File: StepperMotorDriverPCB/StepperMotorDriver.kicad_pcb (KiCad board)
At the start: 4 copper layers, 44.8 x 38.3 mm, 57 parts, among them IC2 TMC2209-LA, J1 Conn_01x02_Pin, J2 Conn_01x01_Pin, J3 Conn_01x01_Pin, J4 Conn_01x04_Socket, J5 USB_C_Receptacle_USB2.0_14P, J6 Conn_01x04_Pin, J7 Conn_01x02_Pin, J8 Conn_01x01_Pin, J9 Conn_01x01_Pin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

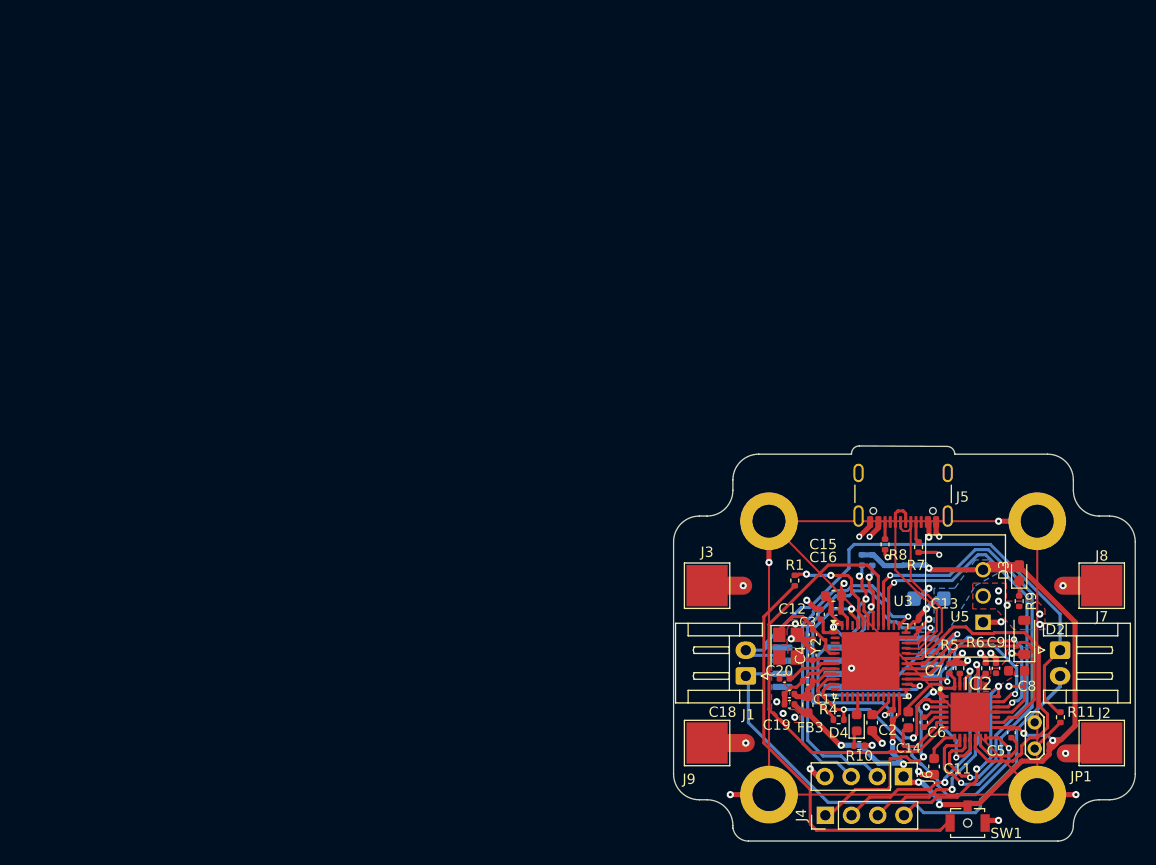
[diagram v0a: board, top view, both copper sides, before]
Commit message: Replaced Microcontrollers and Power Distribution System
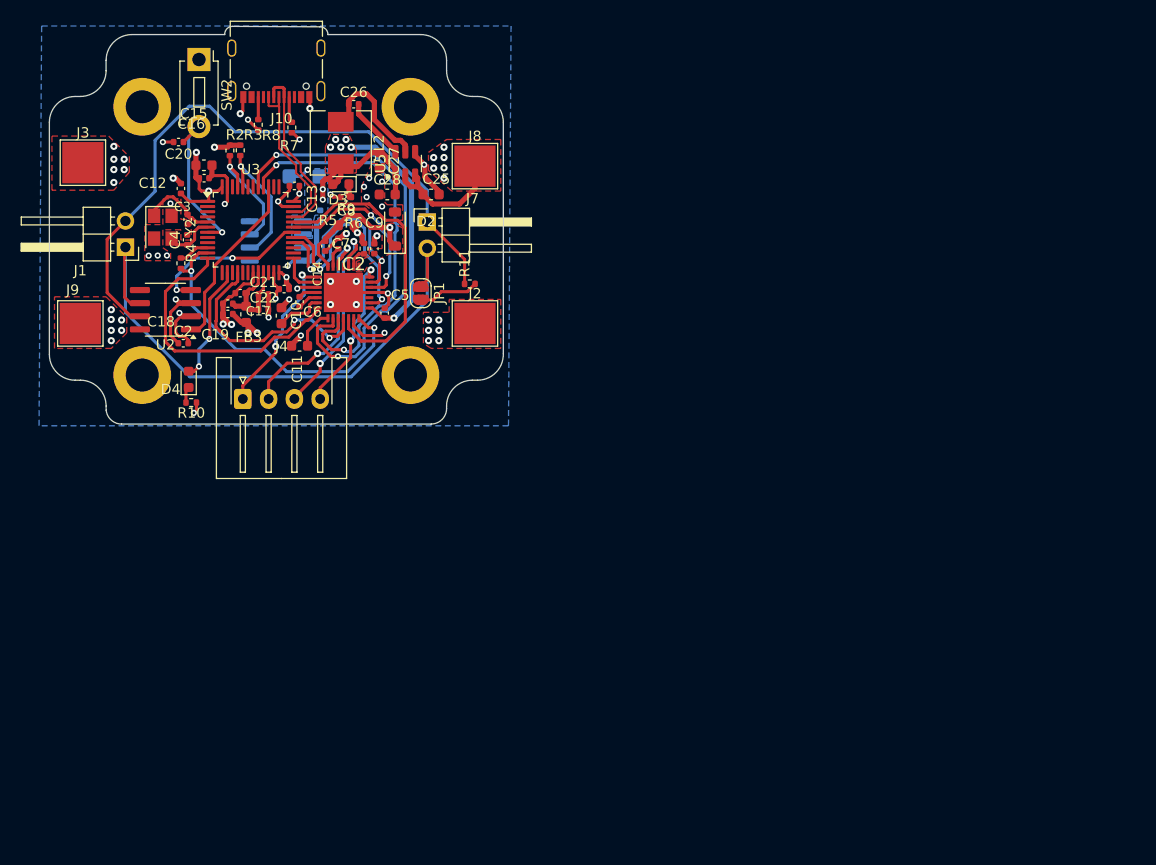
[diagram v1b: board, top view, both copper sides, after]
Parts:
- removed J5: USB_C_Receptacle_USB2.0_14P, Connector_USB:USB_C_Receptacle_GCT_USB4105-xx-A_16P_TopMnt_Horizontal
- removed J6: Conn_01x04_Pin, Connector_PinHeader_2.54mm:PinHeader_1x04_P2.54mm_Vertical
- removed R1: 10K, Resistor_SMD:R_0402_1005Metric
- removed SW1: SW_SPDT, Button_Switch_SMD:SW_SPST_B3U-1100P-B
- added C21: 100n, Capacitor_SMD:C_0402_1005Metric, F.Cu at (72.0, 68.5)
- added C22: 1u, Capacitor_SMD:C_0402_1005Metric, F.Cu at (72.0, 70.0)
- added C25: 10uF, Capacitor_SMD:C_0603_1608Metric, F.Cu at (88.2, 58.8)
- added C26: 100nF, Capacitor_SMD:C_0402_1005Metric, F.Cu at (80.8, 50.1)
- added C27: 22uF, Capacitor_SMD:C_0603_1608Metric, F.Cu at (83.2, 55.6)
- added C28: 22uF, Capacitor_SMD:C_0603_1608Metric, F.Cu at (84.0, 58.8)
- added J10: USB_C_Receptacle_USB2.0_16P, Connector_USB:USB_C_Receptacle_Palconn_UTC16-G, F.Cu at (73.2, 46.9)
- added L2: 4.7uF, Inductor_SMD:L_Chilisin_BMRA00050530, F.Cu at (79.5, 53.8)
- added SW2: SW_SPST, Button_Switch_THT:SW_PUSH_1P1T_6x3.5mm_H5.0_APEM_MJTP1250, F.Cu at (65.8, 45.8)
- C2: value 2.2uF -> 100nF; footprint Capacitor_SMD:C_0603_1608Metric -> Capacitor_SMD:C_0402_1005Metric
- C20: value 100n -> 0.1u
- J1, J7: footprint Connector_JST:JST_EH_S2B-EH_1x02_P2.50mm_Horizontal -> Connector_PinHeader_2.54mm:PinHeader_1x02_P2.54mm_Horizontal
- J4: footprint Connector_PinHeader_2.54mm:PinHeader_1x04_P2.54mm_Vertical -> Connector_JST:JST_XH_S4B-XH-A-1_1x04_P2.50mm_Horizontal
- JP1: footprint TestPoint:TestPoint_2Pads_Pitch2.54mm_Drill0.8mm -> Jumper:SolderJumper-2_P1.3mm_Open_RoundedPad1.0x1.5mm
- R2, R3: value 5K -> 5.1k; moved to F.Cu
- R9: value 1k5 -> 1.5k
- U2: moved to F.Cu
- U3: value STM32F423CHU6 -> STM32G473CBTx; footprint Package_DFN_QFN:QFN-48-1EP_7x7mm_P0.5mm_EP5.6x5.6mm -> Package_QFP:LQFP-48_7x7mm_P0.5mm
- U5: value TSR1-2433E -> AP63203WU; footprint Converter_DCDC:Converter_DCDC_TRACO_TSR1-xxxxE_THT -> Package_TO_SOT_SMD:TSOT-23-6
- moved C20 78.4 mm to (63.8, 53.8), turned to 180 degrees
- moved C8 78.0 mm to (80.0, 61.8)
- moved R4 77.6 mm to (64.0, 65.5), turned to 90 degrees
- moved C2 76.2 mm to (64.2, 73.2), turned to 0 degrees
- moved R9 76.1 mm to (80.0, 59.1), turned to 180 degrees
- moved D3 75.8 mm to (79.5, 57.8), turned to 180 degrees
- moved C12 74.5 mm to (64.0, 58.2)
- moved C16 74.3 mm to (66.2, 57.2)
- moved J7 74.1 mm to (87.9, 61.5), turned to 0 degrees
- moved C15 73.9 mm to (66.2, 56.0)
- moved C13 73.9 mm to (75.0, 58.0), turned to 180 degrees
- moved R2 73.8 mm to (68.8, 54.6)
- moved C11 73.8 mm to (75.5, 73.5), turned to 0 degrees
- moved C1 73.5 mm to (77.5, 60.9)
- moved U3 73.2 mm to (70.8, 62.2)
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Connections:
- C2 pad 1: Net-(U3-VCAP_1) -> +3V3
- C20 pad 1: GND -> Net-(SW2-B)
- C20 pad 2: /RST -> GND
- U3 pad 12: unconnected-(U3-PA2-Pad12) -> /MOT_SPREAD
- U3 pad 14: unconnected-(U3-PA4-Pad14) -> Net-(D4-A)
- U3 pad 16: Net-(D4-A) -> /MOT_DIAG
- U3 pad 19: unconnected-(U3-PB1-Pad19) -> GND
- U3 pad 20: unconnected-(U3-PB2-Pad20) -> +3.3VA
- U3 pad 21: unconnected-(U3-PB10-Pad21) -> +3.3VA
- U3 pad 22: Net-(U3-VCAP_1) -> unconnected-(U3-PB10-Pad22)
- U3 pad 25: /CAN_TX -> /MOT_ENABLE
- U3 pad 26: /CAN_RX -> unconnected-(U3-PB12-Pad26)
- U3 pad 27: /MOT_STBY -> unconnected-(U3-PB13-Pad27)
- U3 pad 28: /MOT_STEP -> /MOT_STBY
- U3 pad 29: /MOT_DIR -> /MOT_STEP
- U3 pad 30: /MOT_DIAG -> /CAN_RX
- U3 pad 31: /MOT_INDEX -> /MOT_DIR
- U3 pad 32: /USB_D- -> /MOT_INDEX
- U3 pad 33: /USB_D+ -> /USB_D-
- U3 pad 34: /SWDIO -> /USB_D+
- U3 pad 37: /SWDCLK -> unconnected-(U3-PA13-Pad37)
- U3 pad 39: /MOT_MS2 -> /CAN_TX
- U3 pad 40: /MOT_MS1 -> /MOT_MS2
- U3 pad 41: /MOT_SPREAD -> /MOT_MS1
- U3 pad 42: /ESCL -> unconnected-(U3-PB5-Pad42)
- U3 pad 43: /ESDA -> unconnected-(U3-PB6-Pad43)
- U3 pad 44: /BOOT0 -> /ESDA
- U3 pad 45: /MOT_ENABLE -> /ESCL
- U3 pad 7: /RST -> Net-(SW2-B)
- U3 pad 8: GND -> unconnected-(U3-PA0-Pad8)
- U3 pad 9: +3.3VA -> unconnected-(U3-PA1-Pad9)
- U5 pad 1: VCC -> +3V3
- U5 pad 2: GND -> VCC
- U5 pad 3: +3V3 -> VCC
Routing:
- net +3V3: track 126.0 -> 66.5 mm, vias 10 -> 16
- net Net-(SW1-B): track 40.4 -> 0.00 mm
- net /SWDIO: track 38.3 -> 0.00 mm, vias 1 -> 0
- net /SWDCLK: track 32.6 -> 0.00 mm, vias 1 -> 0
- net /MOT_ENABLE: track 31.7 -> 4.35 mm, vias 2 -> 0
- net GND: track 99.0 -> 72.3 mm, vias 39 -> 50
- net /MOT_SPREAD: track 46.2 -> 27.7 mm
- net Net-(SW2-B): track 0.00 -> 16.0 mm, vias 0 -> 1
- net Net-(U5-SW): track 0.00 -> 12.1 mm
- net /BOOT0: track 10.7 -> 0.00 mm, vias 2 -> 0
- net Net-(D4-A): track 1.80 -> 11.4 mm, vias 0 -> 2
- net /CANH: track 53.8 -> 62.6 mm
- net VCC: track 18.2 -> 26.7 mm, vias 4 -> 14
- net /MOT_MS2: track 46.6 -> 40.4 mm
- net Net-(U5-BST): track 0.00 -> 6.09 mm
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- added copper zone on F.Cu, net +3V3
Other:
- board size 44.8 x 38.3 mm -> 44 x 38.5 mm

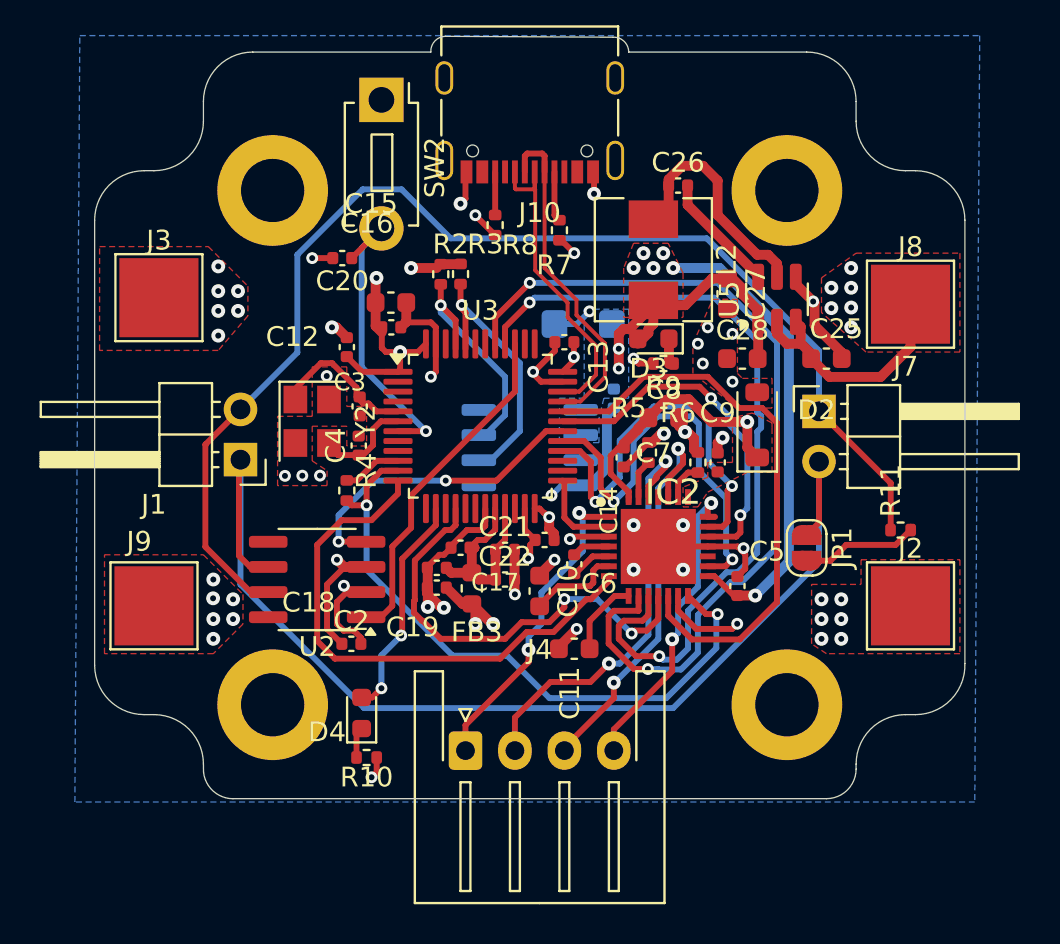
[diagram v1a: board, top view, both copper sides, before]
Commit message: Adjusted CAN passthroughh
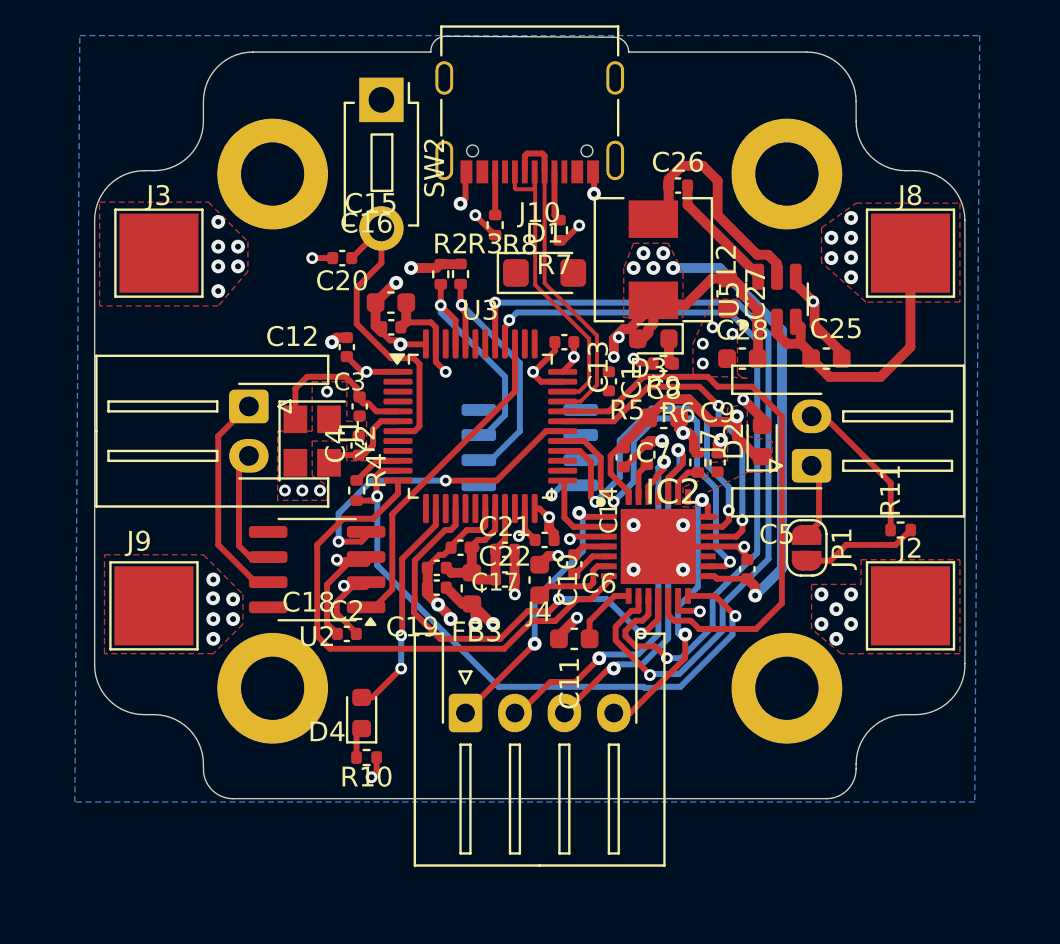
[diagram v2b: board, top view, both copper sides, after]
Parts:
- C1, D1: moved to F.Cu
- D2: footprint Diode_SMD:D_SOD-123 -> Diode_SMD:D_0603_1608Metric
- J1, J7: footprint Connector_PinHeader_2.54mm:PinHeader_1x02_P2.54mm_Horizontal -> Connector_JST:JST_XH_S2B-XH-A-1_1x02_P2.50mm_Horizontal
- moved D1 3.24 mm to (74.0, 54.5), turned to 0 degrees
- moved J7 2.78 mm to (87.5, 64.2), turned to 90 degrees
- moved J1 2.72 mm to (59.0, 61.2), turned to -90 degrees
- moved J8 2.58 mm to (92.5, 53.5)
- moved J3 2.25 mm to (54.5, 53.5)
- moved J4 1.90 mm to (70.0, 76.8)
- moved Y2 1.00 mm to (62.2, 63.0)
- moved C5 0.99 mm to (84.2, 69.5)
- moved C1 0.91 mm to (77.2, 60.0)
- moved D2 0.86 mm to (85.0, 63.0)
- moved H1 0.83 mm to (86.2, 49.5)
- moved H2 0.83 mm to (86.2, 75.5)
- moved H3 0.83 mm to (60.2, 49.5)
- moved H4 0.83 mm to (60.2, 75.5)
- moved C10 0.56 mm to (73.8, 70.0)
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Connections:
- J1 pad 1: /CANL -> /CANH
- J1 pad 2: /CANH -> /CANL
- J7 pad 1: /CANH -> /CANL
- J7 pad 2: /CANL -> /CANH
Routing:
- net /CANL: track 57.7 -> 41.1 mm
- net /CANH: track 62.6 -> 48.1 mm
- net GND: track 72.3 -> 64.2 mm, vias 50 -> 49
- net +3V3: track 66.5 -> 63.7 mm, vias 16 -> 17
- net /OB2: track 16.2 -> 14.2 mm
- net /MOT_MS2: track 40.4 -> 38.5 mm
- net VCC: track 26.7 -> 28.6 mm
- net /MOT_MS1: track 44.7 -> 42.8 mm
- net /OB1: track 21.5 -> 19.9 mm
- net /OA1: track 20.7 -> 19.4 mm
- net /OA2: track 15.8 -> 14.9 mm
- net Net-(SW2-B): track 16.0 -> 16.7 mm, vias 1 -> 0
- net /MOT_SPREAD: track 27.7 -> 27.1 mm
- net Net-(IC2-5VOUT): track 3.90 -> 3.40 mm
- net /MOT_UART_TX: track 3.00 -> 2.50 mm

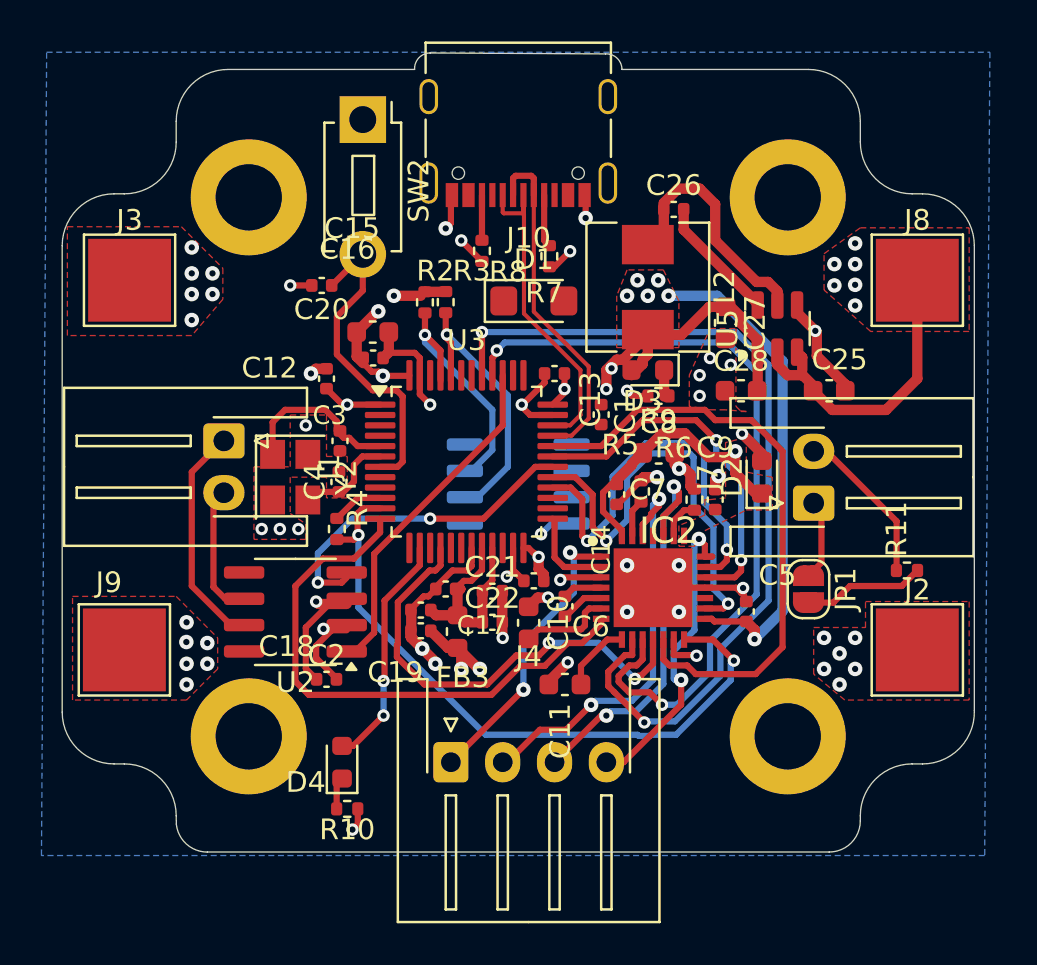
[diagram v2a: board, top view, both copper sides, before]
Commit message: Major changes to layout
Made everything but encoder on top layer. Changed to stronger MC, new buttons, etc.
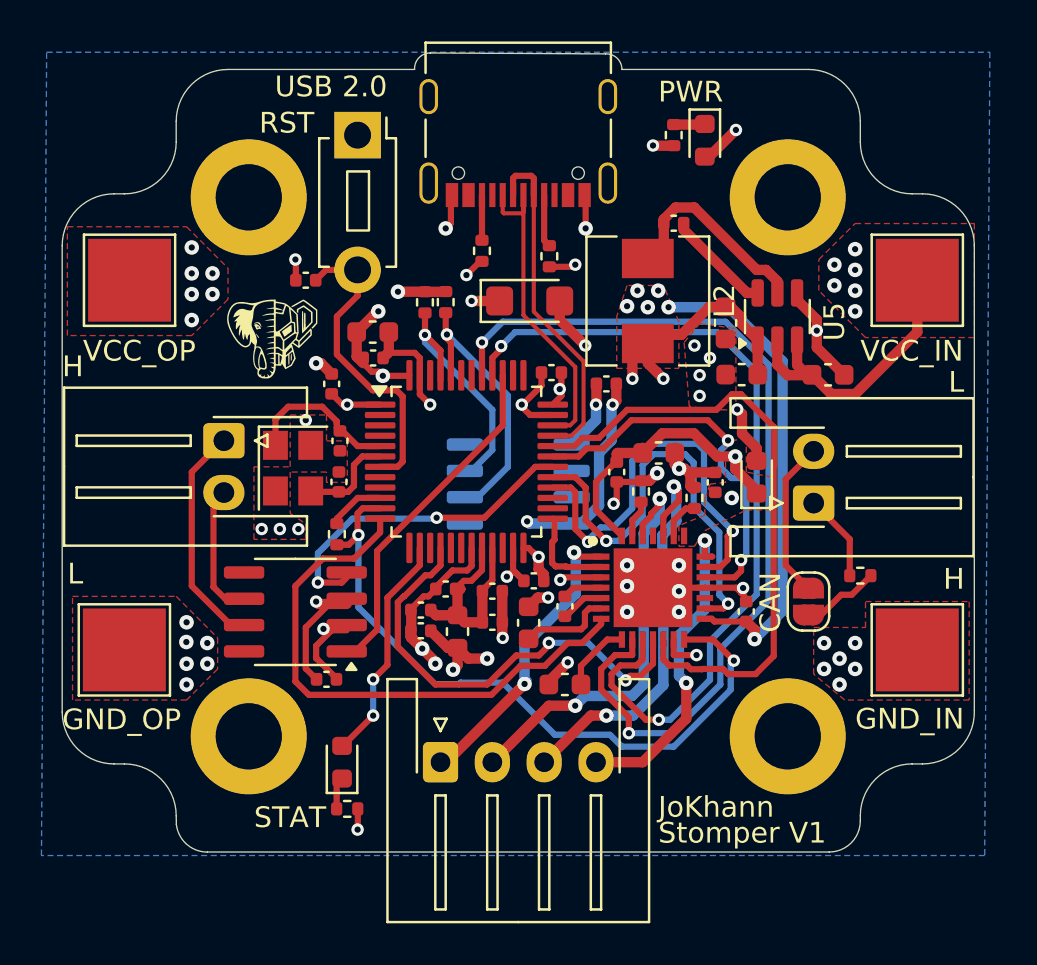
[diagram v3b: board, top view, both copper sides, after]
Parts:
- added G***: LOGO, BTMP:btmp, F.Cu at (61.5, 56.2)
- moved R9 12.6 mm to (80.8, 46.5), turned to -90 degrees
- moved D3 11.4 mm to (82.2, 46.8), turned to -90 degrees
- moved R11 2.26 mm to (89.8, 67.8)
- moved C1 1.50 mm to (77.5, 58.5), turned to 0 degrees
- moved C7 1.08 mm to (78.0, 62.8)
- moved C9 0.83 mm to (82.8, 63.2)
- moved C20 0.81 mm to (63.0, 53.5)
- moved SW2 0.79 mm to (65.5, 46.5)
- moved C28 0.78 mm to (84.0, 58.1)
- moved C25 0.77 mm to (88.2, 58.1)
- moved C26 0.67 mm to (80.8, 50.8)
- moved L2 0.67 mm to (79.5, 54.5)
- moved JP1 0.60 mm to (87.2, 69.0)
- moved U5 0.58 mm to (85.8, 55.2)
- moved J4 0.50 mm to (69.5, 76.8)
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- renumbered J9 to J2, J8 to J3, J3 to J8, J2 to J9
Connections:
- J7 pad 1: /CANL -> /CANH
- J7 pad 2: /CANH -> /CANL
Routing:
- net GND: track 64.2 -> 77.5 mm, vias 49 -> 53
- net /CANL: track 41.1 -> 49.1 mm
- net +3V3: track 63.7 -> 68.3 mm, vias 17 -> 20
- net Net-(JP1-B): track 6.06 -> 3.80 mm
- net Net-(U5-SW): track 12.1 -> 9.96 mm
- net /MOT_MS1: track 42.8 -> 44.9 mm
- net /MOT_MS2: track 38.5 -> 40.6 mm
- net /CANH: track 48.1 -> 50.0 mm
- net Net-(SW2-B): track 16.7 -> 15.1 mm
- net /MOT_DIR: track 17.7 -> 18.8 mm
- net Net-(U5-BST): track 6.09 -> 5.15 mm
- net /MOT_UART_RX: track 32.3 -> 33.2 mm
- net /OA1: track 19.4 -> 20.1 mm
- net /MOT_INDEX: track 29.6 -> 30.4 mm
- net /OA2: track 14.9 -> 15.6 mm
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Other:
- board text added: "CAN"
- board text added: "GND_IN"
- board text added: "GND_OP"
- board text added: "H"
- board text added: "JoKhann"
- board text added: "L"
- board text added: "PWR"
- board text added: "RST"
- board text added: "STAT"
- board text added: "Stomper V1"
- board text added: "USB 2.0"
- board text added: "VCC_IN"
- board text added: "VCC_OP"
